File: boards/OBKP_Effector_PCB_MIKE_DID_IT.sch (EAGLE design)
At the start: 34 parts

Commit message: put fan vcc (12v!) on separate pin from led vcc (5v)
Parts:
- renumbered HOTHEDR to HOT_HEADER
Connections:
- new net N$15: FAN_VCC+.P$1, HOT_HEADER.1
- net FAN_VCC: now also HOT_HEADER.3; no longer FAN_VCC+.P$1, HOT_HEADER.1
- net N$11: now also HOT_HEADER.8; no longer HOT_HEADER.4
- net N$19: now also HOT_HEADER.4; no longer HOT_HEADER.3
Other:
- moved on the sheet: FAN_VCC+
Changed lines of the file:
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@@
 <?xml version="1.0" encoding="utf-8"?>
 <!DOCTYPE eagle SYSTEM "eagle.dtd">
-<eagle version="6.4">
+<eagle version="6.5.0">
 <drawing>
 <settings>
@@
 <part name="GND5" library="SparkFun-Aesthetics" deviceset="GND" device=""/>
 <part name="HOT+" library="OBKP_Effector_PCB" deviceset="LUG" device="3-X"/>
-<part name="HOTHEDR" library="SparkFun-Connectors" deviceset="M05X2" device="RA"/>
+<part name="HOT_HEADER" library="SparkFun-Connectors" deviceset="M05X2" device="RA"/>
 <part name="PROBE-" library="OBKP_Effector_PCB" deviceset="LUG" device="3-X"/>
 <part name="PROBE+" library="OBKP_Effector_PCB" deviceset="LUG" device="3-X"/>
@@
 <attribute name="NAME" x="60.96" y="33.02" size="1.778" layer="95" rot="R90"/>
 </instance>
-<instance part="FAN_VCC+" gate="G$1" x="15.24" y="83.82" smashed="yes">
-<attribute name="NAME" x="20.32" y="91.44" size="1.778" layer="95"/>
+<instance part="FAN_VCC+" gate="G$1" x="22.86" y="83.82" smashed="yes">
+<attribute name="NAME" x="27.94" y="91.44" size="1.778" layer="95"/>
 </instance>
 <instance part="FAN_VCC-" gate="G$1" x="71.12" y="20.32" smashed="yes">
@@
 <attribute name="NAME" x="76.2" y="63.5" size="1.778" layer="95"/>
 </instance>
-<instance part="HOTHEDR" gate="G$1" x="38.1" y="73.66"/>
+<instance part="HOT_HEADER" gate="G$1" x="38.1" y="73.66"/>
 <instance part="PROBE-" gate="G$1" x="40.64" y="20.32" smashed="yes">
 <attribute name="NAME" x="40.64" y="33.02" size="1.778" layer="95" rot="R90"/>
@@
 <pinref part="GND1" gate="1" pin="GND"/>
 <wire x1="25.4" y1="66.04" x2="25.4" y2="73.66" width="0.1524" layer="91"/>
-<pinref part="HOTHEDR" gate="G$1" pin="5"/>
+<pinref part="HOT_HEADER" gate="G$1" pin="5"/>
 <wire x1="25.4" y1="73.66" x2="30.48" y2="73.66" width="0.1524" layer="91"/>
 </segment>
@@
 <pinref part="GND2" gate="1" pin="GND"/>
 <wire x1="48.26" y1="66.04" x2="48.26" y2="73.66" width="0.1524" layer="91"/>
-<pinref part="HOTHEDR" gate="G$1" pin="6"/>
+<pinref part="HOT_HEADER" gate="G$1" pin="6"/>
 <wire x1="48.26" y1="73.66" x2="45.72" y2="73.66" width="0.1524" layer="91"/>
 </segment>
@@
 <wire x1="7.62" y1="76.2" x2="15.24" y2="76.2" width="0.1524" layer="91"/>
 <junction x="7.62" y="76.2"/>
-<pinref part="FAN_VCC+" gate="G$1" pin="P$1"/>
-<wire x1="15.24" y1="83.82" x2="15.24" y2="76.2" width="0.1524" layer="91"/>
+<wire x1="15.24" y1="38.1" x2="15.24" y2="76.2" width="0.1524" layer="91"/>
+<pinref part="HOT_HEADER" gate="G$1" pin="3"/>
+<wire x1="15.24" y1="76.2" x2="30.48" y2="76.2" width="0.1524" layer="91"/>
 <junction x="15.24" y="76.2"/>
-<wire x1="15.24" y1="38.1" x2="15.24" y2="76.2" width="0.1524" layer="91"/>
-<wire x1="15.24" y1="76.2" x2="20.32" y2="76.2" width="0.1524" layer="91"/>
-<wire x1="20.32" y1="76.2" x2="20.32" y2="78.74" width="0.1524" layer="91"/>
-<pinref part="HOTHEDR" gate="G$1" pin="1"/>
-<wire x1="20.32" y1="78.74" x2="30.48" y2="78.74" width="0.1524" layer="91"/>
 </segment>
 </net>
 <net name="N$8" class="0">
 <segment>
-<pinref part="HOTHEDR" gate="G$1" pin="2"/>
+<pinref part="HOT_HEADER" gate="G$1" pin="2"/>
 <wire x1="45.72" y1="78.74" x2="63.5" y2="78.74" width="0.1524" layer="91"/>
 <pinref part="HOT-" gate="G$1" pin="P$1"/>
@@
 <net name="N$10" class="0">
 <segment>
-<pinref part="HOTHEDR" gate="G$1" pin="10"/>
+<pinref part="HOT_HEADER" gate="G$1" pin="10"/>
 <pinref part="HOT+" gate="G$1" pin="P$1"/>
 <wire x1="45.72" y1="68.58" x2="63.5" y2="68.58" width="0.1524" layer="91"/>
@@
 </segment>
 </net>
-<net name="N$11" class="0">
-<segment>
-<pinref part="THERM+" gate="G$1" pin="P$1"/>
-<wire x1="55.88" y1="71.12" x2="63.5" y2="71.12" width="0.1524" layer="91"/>
-<pinref part="HOTHEDR" gate="G$1" pin="4"/>
-<wire x1="45.72" y1="76.2" x2="55.88" y2="76.2" width="0.1524" layer="91"/>
-<wire x1="55.88" y1="76.2" x2="55.88" y2="71.12" width="0.1524" layer="91"/>
-</segment>
-</net>
 <net name="N$19" class="0">
 <segment>
 <pinref part="PROBE+" gate="G$1" pin="P$1"/>
 <wire x1="63.5" y1="93.98" x2="60.96" y2="93.98" width="0.1524" layer="91"/>
-<wire x1="60.96" y1="93.98" x2="60.96" y2="83.82" width="0.1524" layer="91"/>
-<wire x1="60.96" y1="83.82" x2="25.4" y2="83.82" width="0.1524" layer="91"/>
-<wire x1="25.4" y1="83.82" x2="25.4" y2="76.2" width="0.1524" layer="91"/>
-<pinref part="HOTHEDR" gate="G$1" pin="3"/>
-<wire x1="25.4" y1="76.2" x2="30.48" y2="76.2" width="0.1524" layer="91"/>
+<wire x1="60.96" y1="93.98" x2="60.96" y2="76.2" width="0.1524" layer="91"/>
+<pinref part="HOT_HEADER" gate="G$1" pin="4"/>
+<wire x1="60.96" y1="76.2" x2="45.72" y2="76.2" width="0.1524" layer="91"/>
 </segment>
 </net>
@@
 <wire x1="63.5" y1="55.88" x2="22.86" y2="55.88" width="0.1524" layer="91"/>
 <wire x1="22.86" y1="55.88" x2="22.86" y2="71.12" width="0.1524" layer="91"/>
-<pinref part="HOTHEDR" gate="G$1" pin="7"/>
+<pinref part="HOT_HEADER" gate="G$1" pin="7"/>
 <wire x1="30.48" y1="71.12" x2="22.86" y2="71.12" width="0.1524" layer="91"/>
 </segment>
@@
 <wire x1="50.8" y1="81.28" x2="50.8" y2="58.42" width="0.1524" layer="91"/>
 <wire x1="50.8" y1="58.42" x2="30.48" y2="58.42" width="0.1524" layer="91"/>
-<pinref part="HOTHEDR" gate="G$1" pin="9"/>
+<pinref part="HOT_HEADER" gate="G$1" pin="9"/>
 <wire x1="30.48" y1="58.42" x2="30.48" y2="68.58" width="0.1524" layer="91"/>
 <junction x="50.8" y="81.28"/>
 </segment>
 </net>
+<net name="N$11" class="0">
+<segment>
+<pinref part="THERM+" gate="G$1" pin="P$1"/>
+<pinref part="HOT_HEADER" gate="G$1" pin="8"/>
+<wire x1="63.5" y1="71.12" x2="45.72" y2="71.12" width="0.1524" layer="91"/>
+</segment>
+</net>
+<net name="N$15" class="0">
+<segment>
+<pinref part="FAN_VCC+" gate="G$1" pin="P$1"/>
+<wire x1="22.86" y1="83.82" x2="22.86" y2="78.74" width="0.1524" layer="91"/>
+<pinref part="HOT_HEADER" gate="G$1" pin="1"/>
+<wire x1="22.86" y1="78.74" x2="30.48" y2="78.74" width="0.1524" layer="91"/>
+</segment>
+</net>

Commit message: put third fan pwm pin on same net as other two
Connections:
- removed net N$12: FAN_PWM+.P$1, FAN_PWM2+.P$1, HOT_HEADER.9
- net GND: no longer HOT_HEADER.6
- net N$10: now also HOT_HEADER.8
- net N$11: now also HOT_HEADER.7; no longer HOT_HEADER.8
- net N$15: now also FAN_PWM+.P$1, FAN_PWM2+.P$1
- net N$19: now also HOT_HEADER.6; no longer HOT_HEADER.4
- net N$20: now also HOT_HEADER.9; no longer HOT_HEADER.7
- net N$8: now also HOT_HEADER.4
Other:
- moved on the sheet: FAN_PWM+, FAN_PWM2+, FAN_VCC+
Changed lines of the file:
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@@
 <part name="FAN_VCC-" library="OBKP_Effector_PCB" deviceset="LUG" device="2.3"/>
 <part name="GND1" library="SparkFun-Aesthetics" deviceset="GND" device=""/>
-<part name="GND2" library="SparkFun-Aesthetics" deviceset="GND" device=""/>
 <part name="GND3" library="SparkFun-Aesthetics" deviceset="GND" device=""/>
 <part name="GND4" library="SparkFun-Aesthetics" deviceset="GND" device=""/>
@@
 <attribute name="NAME" x="76.2" y="55.88" size="1.778" layer="95"/>
 </instance>
-<instance part="FAN_PWM+" gate="G$1" x="58.42" y="83.82" smashed="yes">
-<attribute name="NAME" x="58.42" y="96.52" size="1.778" layer="95" rot="R90"/>
+<instance part="FAN_PWM+" gate="G$1" x="53.34" y="88.9" smashed="yes">
+<attribute name="NAME" x="53.34" y="101.6" size="1.778" layer="95" rot="R90"/>
 </instance>
 <instance part="FAN_PWM-" gate="G$1" x="50.8" y="20.32" smashed="yes">
 <attribute name="NAME" x="50.8" y="33.02" size="1.778" layer="95" rot="R90"/>
 </instance>
-<instance part="FAN_PWM2+" gate="G$1" x="50.8" y="83.82" smashed="yes">
-<attribute name="NAME" x="50.8" y="96.52" size="1.778" layer="95" rot="R90"/>
+<instance part="FAN_PWM2+" gate="G$1" x="45.72" y="88.9" smashed="yes">
+<attribute name="NAME" x="45.72" y="101.6" size="1.778" layer="95" rot="R90"/>
 </instance>
 <instance part="FAN_PWM2-" gate="G$1" x="60.96" y="20.32" smashed="yes">
 <attribute name="NAME" x="60.96" y="33.02" size="1.778" layer="95" rot="R90"/>
 </instance>
-<instance part="FAN_VCC+" gate="G$1" x="22.86" y="83.82" smashed="yes">
-<attribute name="NAME" x="27.94" y="91.44" size="1.778" layer="95"/>
+<instance part="FAN_VCC+" gate="G$1" x="38.1" y="88.9" smashed="yes">
+<attribute name="NAME" x="43.18" y="96.52" size="1.778" layer="95"/>
 </instance>
 <instance part="FAN_VCC-" gate="G$1" x="71.12" y="20.32" smashed="yes">
@@
 </instance>
 <instance part="GND1" gate="1" x="25.4" y="63.5"/>
-<instance part="GND2" gate="1" x="48.26" y="63.5"/>
 <instance part="GND3" gate="1" x="-17.78" y="43.18"/>
 <instance part="GND4" gate="1" x="50.8" y="12.7"/>
@@
 <pinref part="HOT_HEADER" gate="G$1" pin="5"/>
 <wire x1="25.4" y1="73.66" x2="30.48" y2="73.66" width="0.1524" layer="91"/>
-</segment>
-<segment>
-<pinref part="GND2" gate="1" pin="GND"/>
-<wire x1="48.26" y1="66.04" x2="48.26" y2="73.66" width="0.1524" layer="91"/>
-<pinref part="HOT_HEADER" gate="G$1" pin="6"/>
-<wire x1="48.26" y1="73.66" x2="45.72" y2="73.66" width="0.1524" layer="91"/>
 </segment>
 </net>
@@
 <segment>
 <pinref part="HOT_HEADER" gate="G$1" pin="2"/>
-<wire x1="45.72" y1="78.74" x2="63.5" y2="78.74" width="0.1524" layer="91"/>
+<wire x1="45.72" y1="78.74" x2="50.8" y2="78.74" width="0.1524" layer="91"/>
 <pinref part="HOT-" gate="G$1" pin="P$1"/>
+<wire x1="50.8" y1="78.74" x2="63.5" y2="78.74" width="0.1524" layer="91"/>
 <wire x1="63.5" y1="78.74" x2="63.5" y2="86.36" width="0.1524" layer="91"/>
+<wire x1="50.8" y1="78.74" x2="50.8" y2="76.2" width="0.1524" layer="91"/>
+<pinref part="HOT_HEADER" gate="G$1" pin="4"/>
+<wire x1="50.8" y1="76.2" x2="45.72" y2="76.2" width="0.1524" layer="91"/>
+<junction x="50.8" y="78.74"/>
 </segment>
 </net>
@@
 <pinref part="HOT_HEADER" gate="G$1" pin="10"/>
 <pinref part="HOT+" gate="G$1" pin="P$1"/>
-<wire x1="45.72" y1="68.58" x2="63.5" y2="68.58" width="0.1524" layer="91"/>
+<wire x1="45.72" y1="68.58" x2="50.8" y2="68.58" width="0.1524" layer="91"/>
+<wire x1="50.8" y1="68.58" x2="63.5" y2="68.58" width="0.1524" layer="91"/>
 <wire x1="63.5" y1="68.58" x2="63.5" y2="63.5" width="0.1524" layer="91"/>
+<wire x1="50.8" y1="68.58" x2="50.8" y2="71.12" width="0.1524" layer="91"/>
+<pinref part="HOT_HEADER" gate="G$1" pin="8"/>
+<wire x1="50.8" y1="71.12" x2="45.72" y2="71.12" width="0.1524" layer="91"/>
+<junction x="50.8" y="68.58"/>
 </segment>
 </net>
@@
 <pinref part="PROBE+" gate="G$1" pin="P$1"/>
 <wire x1="63.5" y1="93.98" x2="60.96" y2="93.98" width="0.1524" layer="91"/>
-<wire x1="60.96" y1="93.98" x2="60.96" y2="76.2" width="0.1524" layer="91"/>
-<pinref part="HOT_HEADER" gate="G$1" pin="4"/>
-<wire x1="60.96" y1="76.2" x2="45.72" y2="76.2" width="0.1524" layer="91"/>
+<wire x1="60.96" y1="93.98" x2="60.96" y2="73.66" width="0.1524" layer="91"/>
+<pinref part="HOT_HEADER" gate="G$1" pin="6"/>
+<wire x1="60.96" y1="73.66" x2="45.72" y2="73.66" width="0.1524" layer="91"/>
 </segment>
 </net>
@@
 <pinref part="THERM-" gate="G$1" pin="P$1"/>
 <wire x1="63.5" y1="55.88" x2="22.86" y2="55.88" width="0.1524" layer="91"/>
-<wire x1="22.86" y1="55.88" x2="22.86" y2="71.12" width="0.1524" layer="91"/>
+<wire x1="22.86" y1="55.88" x2="22.86" y2="68.58" width="0.1524" layer="91"/>
+<pinref part="HOT_HEADER" gate="G$1" pin="9"/>
+<wire x1="22.86" y1="68.58" x2="30.48" y2="68.58" width="0.1524" layer="91"/>
+</segment>
+</net>
+<net name="N$15" class="0">
+<segment>
+<pinref part="FAN_PWM+" gate="G$1" pin="P$1"/>
+<wire x1="53.34" y1="86.36" x2="53.34" y2="88.9" width="0.1524" layer="91"/>
+<pinref part="FAN_PWM2+" gate="G$1" pin="P$1"/>
+<wire x1="45.72" y1="86.36" x2="45.72" y2="88.9" width="0.1524" layer="91"/>
+<wire x1="45.72" y1="86.36" x2="53.34" y2="86.36" width="0.1524" layer="91"/>
+<junction x="45.72" y="86.36"/>
+<pinref part="FAN_VCC+" gate="G$1" pin="P$1"/>
+<wire x1="38.1" y1="88.9" x2="38.1" y2="86.36" width="0.1524" layer="91"/>
+<wire x1="38.1" y1="86.36" x2="45.72" y2="86.36" width="0.1524" layer="91"/>
+<junction x="38.1" y="86.36"/>
+<wire x1="38.1" y1="86.36" x2="27.94" y2="86.36" width="0.1524" layer="91"/>
+<wire x1="27.94" y1="86.36" x2="27.94" y2="78.74" width="0.1524" layer="91"/>
+<pinref part="HOT_HEADER" gate="G$1" pin="1"/>
+<wire x1="27.94" y1="78.74" x2="30.48" y2="78.74" width="0.1524" layer="91"/>
+</segment>
+</net>
+<net name="N$11" class="0">
+<segment>
+<pinref part="THERM+" gate="G$1" pin="P$1"/>
+<wire x1="63.5" y1="71.12" x2="55.88" y2="71.12" width="0.1524" layer="91"/>
+<wire x1="55.88" y1="71.12" x2="55.88" y2="58.42" width="0.1524" layer="91"/>
+<wire x1="55.88" y1="58.42" x2="27.94" y2="58.42" width="0.1524" layer="91"/>
+<wire x1="27.94" y1="58.42" x2="27.94" y2="71.12" width="0.1524" layer="91"/>
 <pinref part="HOT_HEADER" gate="G$1" pin="7"/>
-<wire x1="30.48" y1="71.12" x2="22.86" y2="71.12" width="0.1524" layer="91"/>
-</segment>
-</net>
-<net name="N$12" class="0">
-<segment>
-<pinref part="FAN_PWM+" gate="G$1" pin="P$1"/>
-<wire x1="58.42" y1="81.28" x2="58.42" y2="83.82" width="0.1524" layer="91"/>
-<pinref part="FAN_PWM2+" gate="G$1" pin="P$1"/>
-<wire x1="50.8" y1="81.28" x2="50.8" y2="83.82" width="0.1524" layer="91"/>
-<wire x1="50.8" y1="81.28" x2="58.42" y2="81.28" width="0.1524" layer="91"/>
-<wire x1="50.8" y1="81.28" x2="50.8" y2="58.42" width="0.1524" layer="91"/>
-<wire x1="50.8" y1="58.42" x2="30.48" y2="58.42" width="0.1524" layer="91"/>
-<pinref part="HOT_HEADER" gate="G$1" pin="9"/>
-<wire x1="30.48" y1="58.42" x2="30.48" y2="68.58" width="0.1524" layer="91"/>
-<junction x="50.8" y="81.28"/>
-</segment>
-</net>
-<net name="N$11" class="0">
-<segment>
-<pinref part="THERM+" gate="G$1" pin="P$1"/>
-<pinref part="HOT_HEADER" gate="G$1" pin="8"/>
-<wire x1="63.5" y1="71.12" x2="45.72" y2="71.12" width="0.1524" layer="91"/>
-</segment>
-</net>
-<net name="N$15" class="0">
-<segment>
-<pinref part="FAN_VCC+" gate="G$1" pin="P$1"/>
-<wire x1="22.86" y1="83.82" x2="22.86" y2="78.74" width="0.1524" layer="91"/>
-<pinref part="HOT_HEADER" gate="G$1" pin="1"/>
-<wire x1="22.86" y1="78.74" x2="30.48" y2="78.74" width="0.1524" layer="91"/>
-</segment>
-</net>
+<wire x1="27.94" y1="71.12" x2="30.48" y2="71.12" width="0.1524" layer="91"/>
+</segment>
+</net>

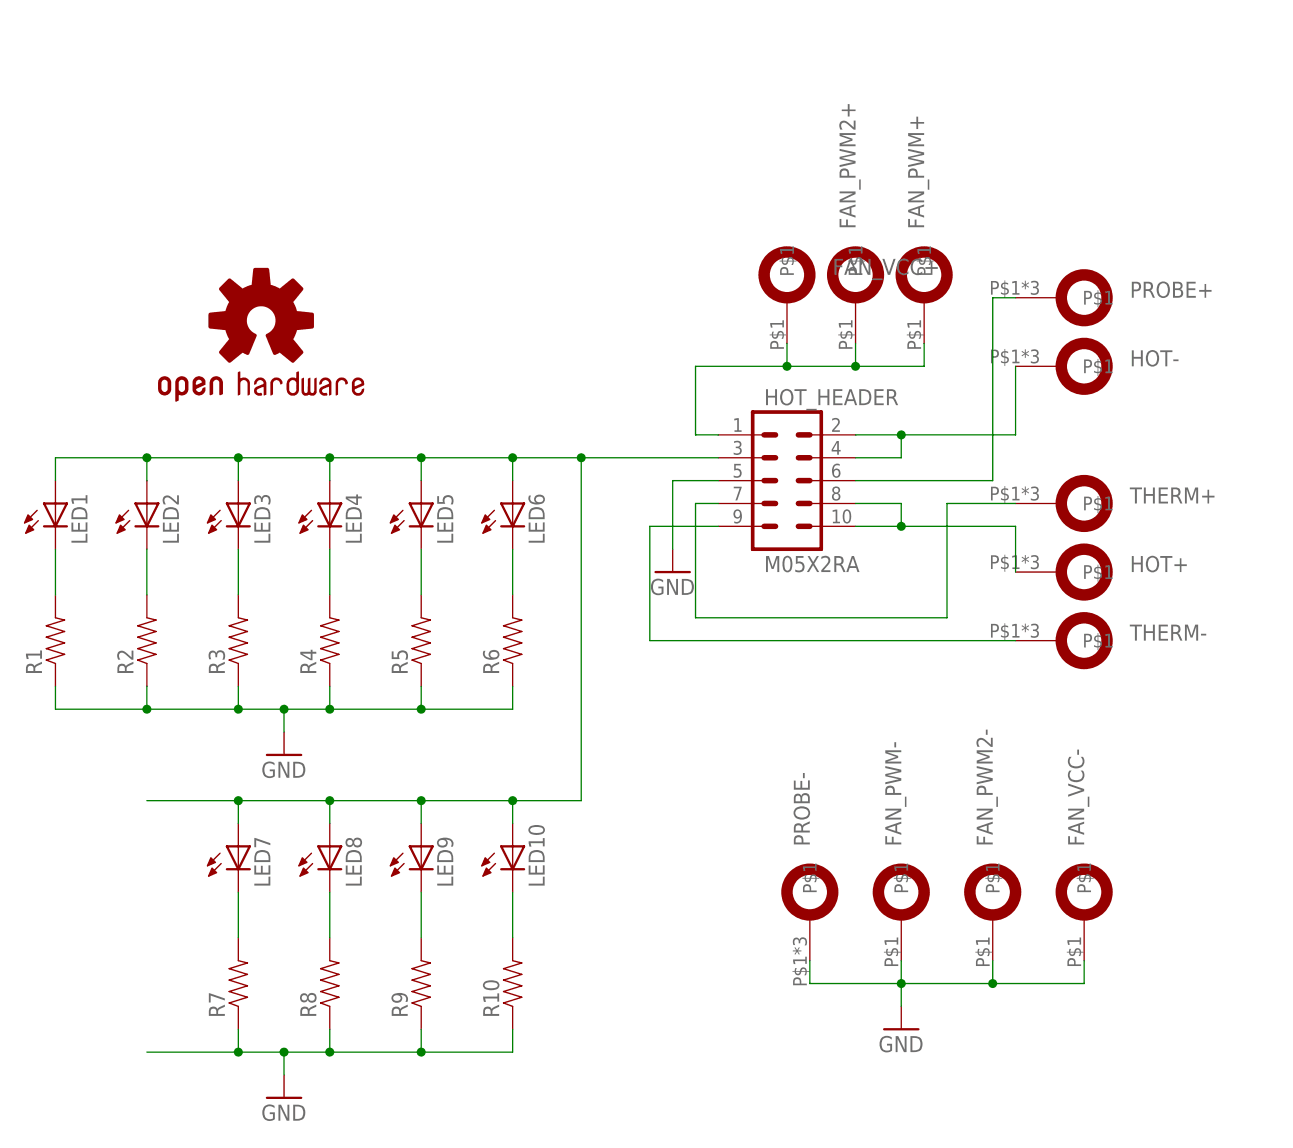
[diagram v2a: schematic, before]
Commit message: moved fan+ to hot+ net and fan- to fan pwm net and rerouted with burlier traces
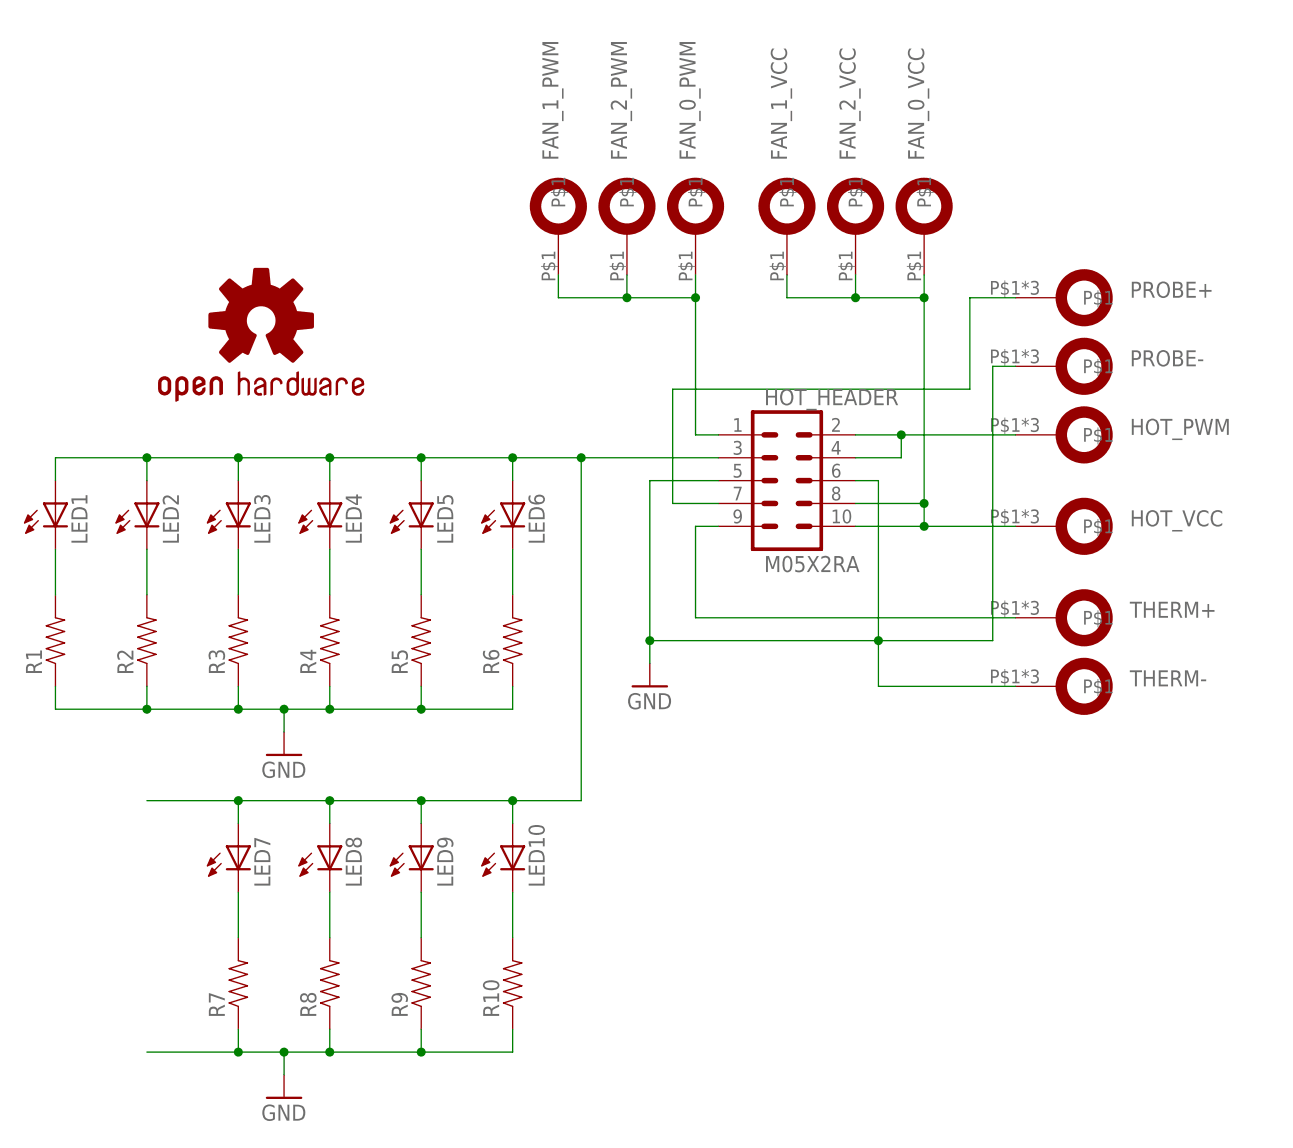
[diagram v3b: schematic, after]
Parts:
- removed FAN_PWM+, FAN_PWM-, FAN_PWM2+, FAN_PWM2-, FAN_VCC+, FAN_VCC-: LUG2.3, OBKP_Effector_PCB:LUG2.3
- removed HOT+, HOT-: LUG3-X, OBKP_Effector_PCB:LUG3-X
- added FAN_0_PWM, FAN_0_VCC, FAN_1_PWM, FAN_1_VCC, FAN_2_PWM, FAN_2_VCC: LUG2.3, OBKP_Effector_PCB:LUG2.3
- added HOT_PWM, HOT_VCC: LUG3-X, OBKP_Effector_PCB:LUG3-X
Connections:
- removed net N$15: FAN_PWM+.P$1, FAN_PWM2+.P$1, FAN_VCC+.P$1, HOT_HEADER.1
- removed net N$19: HOT_HEADER.6, PROBE+.P$1
- removed net N$20: HOT_HEADER.9, THERM-.P$1
- new net N$12: HOT_HEADER.7, PROBE+.P$1
- new net N$17: FAN_0_PWM.P$1, FAN_1_PWM.P$1, FAN_2_PWM.P$1, HOT_HEADER.1
- net GND: now also HOT_HEADER.6, THERM-.P$1; no longer FAN_PWM-.P$1, FAN_PWM2-.P$1, FAN_VCC-.P$1
- net N$10: now also FAN_0_VCC.P$1, FAN_1_VCC.P$1, FAN_2_VCC.P$1, HOT_VCC.P$1; no longer HOT+.P$1
- net N$11: now also HOT_HEADER.9; no longer HOT_HEADER.7
- net N$8: now also HOT_PWM.P$1; no longer HOT-.P$1
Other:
- moved on the sheet: PROBE-, THERM+, THERM-
